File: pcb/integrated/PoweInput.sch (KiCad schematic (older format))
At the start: 35 parts, among them J8001 Conn_01x02_Female, Q8001 Q_NMOS_GDS, Q8002 Q_NMOS_GDS, U8001 SN74LVC1T45DBV, U8002 ADuM5230, U8003 ACS730

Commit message: schematic fixes and component placement
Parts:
- removed U8001: SN74LVC1T45DBV, Package_TO_SOT_SMD:SOT-23-6, symbol Logic_LevelTranslator:SN74LVC1T45DBV
- added C8005: 0.47u, Capacitor_SMD:C_0402_1005Metric, symbol Device:C
- added R8013: 10k, Resistor_SMD:R_0603_1608Metric, symbol Device:R
- added U8001: 74LVC2T45DC, Package_SO:VSSOP-8_2.3x2mm_P0.5mm, symbol Logic_LevelTranslator:74LVC2T45DC
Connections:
- net labels added: SUPPLY_EN1, SUPPLY_EN2
- net labels removed: +3V3D, SUPPLY_EN
- wire segments 135 -> 142
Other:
- moved on the sheet: C8001, R8001
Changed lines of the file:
@@
 Connection ~ 5250 2100
-$Comp
-L Logic_LevelTranslator:SN74LVC1T45DBV U8001
-U 1 1 5D74803E
-P 2350 6300
-F 0 "U8001" H 2791 6346 50  0000 L CNN
-F 1 "SN74LVC1T45DBV" H 2550 5900 50  0000 L CNN
-F 2 "Package_TO_SOT_SMD:SOT-23-6" H 2350 5850 50  0001 C CNN
-F 3 "http://www.ti.com/lit/ds/symlink/sn74lvc1t45.pdf" H 1450 5650 50  0001 C CNN
-	1    2350 6300
-	1    0    0    -1
-$EndComp
 $Comp
 L Device:C C?
 U 1 1 5D748AFA
-P 1800 5500
+P 1250 4800
 AR Path="/5D33C751/5D748AFA" Ref="C?"  Part="1"
 AR Path="/5D688380/5D748AFA" Ref="C8001"  Part="1"
-F 0 "C8001" H 1915 5546 50  0000 L CNN
-F 1 "0.47u" H 1915 5455 50  0000 L CNN
-F 2 "Capacitor_SMD:C_0402_1005Metric" H 1838 5350 50  0001 C CNN
-F 3 "~" H 1800 5500 50  0001 C CNN
-	1    1800 5500
+F 0 "C8001" H 1365 4846 50  0000 L CNN
+F 1 "0.47u" H 1365 4755 50  0000 L CNN
+F 2 "Capacitor_SMD:C_0402_1005Metric" H 1288 4650 50  0001 C CNN
+F 3 "~" H 1250 4800 50  0001 C CNN
+	1    1250 4800
 	1    0    0    -1
 $EndComp
@@
 L power:GND #PWR08004
 U 1 1 5D748F7A
-P 2350 6750
-F 0 "#PWR08004" H 2350 6500 50  0001 C CNN
-F 1 "GND" H 2355 6577 50  0000 C CNN
-F 2 "" H 2350 6750 50  0001 C CNN
-F 3 "" H 2350 6750 50  0001 C CNN
-	1    2350 6750
+P 2350 6950
+F 0 "#PWR08004" H 2350 6700 50  0001 C CNN
+F 1 "GND" H 2500 6900 50  0000 C CNN
+F 2 "" H 2350 6950 50  0001 C CNN
+F 3 "" H 2350 6950 50  0001 C CNN
+	1    2350 6950
 	1    0    0    -1
 $EndComp
@@
 	1    0    0    -1
 $EndComp
-$Comp
-L power:GND #PWR08008
-U 1 1 5D74A979
-P 4000 6500
-F 0 "#PWR08008" H 4000 6250 50  0001 C CNN
-F 1 "GND" H 4005 6327 50  0000 C CNN
-F 2 "" H 4000 6500 50  0001 C CNN
-F 3 "" H 4000 6500 50  0001 C CNN
-	1    4000 6500
-	1    0    0    -1
-$EndComp
-Wire Wire Line
-	4000 6400 4000 6500
-Wire Wire Line
-	4000 6400 4300 6400
 Wire Wire Line
 	4300 6300 2750 6300
@@
 L power:GND #PWR08002
 U 1 1 5D755B60
-P 1800 5700
-F 0 "#PWR08002" H 1800 5450 50  0001 C CNN
-F 1 "GND" H 1805 5527 50  0000 C CNN
-F 2 "" H 1800 5700 50  0001 C CNN
-F 3 "" H 1800 5700 50  0001 C CNN
-	1    1800 5700
-	1    0    0    -1
-$EndComp
-Wire Wire Line
-	1800 5300 1800 5350
-Wire Wire Line
-	1800 5650 1800 5700
-Wire Wire Line
-	2350 6700 2350 6750
+P 1250 5000
+F 0 "#PWR08002" H 1250 4750 50  0001 C CNN
+F 1 "GND" H 1255 4827 50  0000 C CNN
+F 2 "" H 1250 5000 50  0001 C CNN
+F 3 "" H 1250 5000 50  0001 C CNN
+	1    1250 5000
+	1    0    0    -1
+$EndComp
+Wire Wire Line
+	1250 4600 1250 4650
+Wire Wire Line
+	1250 4950 1250 5000
 $Comp
 L power:+3V3 #PWR08003
 U 1 1 5D75B234
-P 1900 6500
-F 0 "#PWR08003" H 1900 6350 50  0001 C CNN
-F 1 "+3V3" V 1915 6628 50  0000 L CNN
-F 2 "" H 1900 6500 50  0001 C CNN
-F 3 "" H 1900 6500 50  0001 C CNN
-	1    1900 6500
-	0    -1   -1   0
-$EndComp
-Wire Wire Line
-	1950 6500 1900 6500
+P 1250 4600
+F 0 "#PWR08003" H 1250 4450 50  0001 C CNN
+F 1 "+3V3" V 1265 4728 50  0000 L CNN
+F 2 "" H 1250 4600 50  0001 C CNN
+F 3 "" H 1250 4600 50  0001 C CNN
+	1    1250 4600
+	1    0    0    -1
+$EndComp
 Wire Wire Line
 	3850 6900 3850 6800
@@
 	1    0    0    -1
 $EndComp
-Text GLabel 1150 6300 0    50   Input ~ 0
-SUPPLY_EN
+Text GLabel 1100 6500 0    50   Input ~ 0
+SUPPLY_EN1
 Wire Wire Line
 	6100 6400 6100 6450
@@
 L Device:R R?
 U 1 1 5D7A4D67
-P 1300 6650
+P 1250 6850
 AR Path="/5D33C751/5D7A4D67" Ref="R?"  Part="1"
 AR Path="/5D688380/5D7A4D67" Ref="R8001"  Part="1"
-F 0 "R8001" H 1370 6696 50  0000 L CNN
-F 1 "10k" H 1370 6605 50  0000 L CNN
-F 2 "Resistor_SMD:R_0603_1608Metric" V 1230 6650 50  0001 C CNN
-F 3 "~" H 1300 6650 50  0001 C CNN
-	1    1300 6650
+F 0 "R8001" H 1320 6896 50  0000 L CNN
+F 1 "10k" H 1320 6805 50  0000 L CNN
+F 2 "Resistor_SMD:R_0603_1608Metric" V 1180 6850 50  0001 C CNN
+F 3 "~" H 1250 6850 50  0001 C CNN
+	1    1250 6850
 	1    0    0    1
 $EndComp
 Wire Wire Line
-	1300 6500 1300 6300
-Wire Wire Line
-	1300 6300 1950 6300
-Wire Wire Line
-	1300 6300 1150 6300
-Connection ~ 1300 6300
+	1250 6700 1250 6500
+Wire Wire Line
+	1250 6500 1100 6500
+Connection ~ 1250 6500
 $Comp
 L power:GND #PWR08001
 U 1 1 5D7AE718
-P 1300 6850
-F 0 "#PWR08001" H 1300 6600 50  0001 C CNN
-F 1 "GND" H 1305 6677 50  0000 C CNN
-F 2 "" H 1300 6850 50  0001 C CNN
-F 3 "" H 1300 6850 50  0001 C CNN
-	1    1300 6850
-	1    0    0    -1
-$EndComp
-Wire Wire Line
-	1300 6800 1300 6850
+P 1250 7050
+F 0 "#PWR08001" H 1250 6800 50  0001 C CNN
+F 1 "GND" H 1255 6877 50  0000 C CNN
+F 2 "" H 1250 7050 50  0001 C CNN
+F 3 "" H 1250 7050 50  0001 C CNN
+	1    1250 7050
+	1    0    0    -1
+$EndComp
+Wire Wire Line
+	1250 7000 1250 7050
 $Comp
 L wbraun_ic_lib:ACS730 U8003
@@
 Text GLabel 7700 5100 0    50   Input ~ 0
 IL_ZERO
-Text GLabel 1800 5300 0    50   Input ~ 0
-+3V3D
-Text GLabel 2250 5800 1    50   Input ~ 0
-+3V3D
 $Comp
 L Device:R R?
@@
 Wire Wire Line
 	9700 3300 9700 3500
-Text Label 5000 1950 0    50   ~ 0
-VIN
 Text Label 5450 6750 0    50   ~ 0
 GATE2+
@@
 Wire Wire Line
 	9700 3900 9700 4150
+Text GLabel 5000 1950 2    50   Input ~ 0
+VIN
+$Comp
+L Logic_LevelTranslator:74LVC2T45DC U8001
+U 1 1 5D8F7B18
+P 2350 6400
+F 0 "U8001" H 2650 6900 50  0000 C CNN
+F 1 "74LVC2T45DC" H 1900 5950 50  0000 C CNN
+F 2 "Package_SO:VSSOP-8_2.3x2mm_P0.5mm" H 2350 5550 50  0001 C CNN
+F 3 "https://assets.nexperia.com/documents/data-sheet/74LVC_LVCH2T45.pdf" H 2600 6150 50  0001 C CNN
+	1    2350 6400
+	1    0    0    -1
+$EndComp
+Wire Wire Line
+	2950 6400 2950 6500
+Wire Wire Line
+	2950 6500 2750 6500
+Wire Wire Line
+	2950 6400 4300 6400
+$Comp
+L power:+3V3 #PWR0180
+U 1 1 5D909304
+P 2250 5800
+F 0 "#PWR0180" H 2250 5650 50  0001 C CNN
+F 1 "+3V3" V 2265 5928 50  0000 L CNN
+F 2 "" H 2250 5800 50  0001 C CNN
+F 3 "" H 2250 5800 50  0001 C CNN
+	1    2250 5800
+	1    0    0    -1
+$EndComp
+$Comp
+L Device:C C?
+U 1 1 5D90B099
+P 1950 4800
+AR Path="/5D33C751/5D90B099" Ref="C?"  Part="1"
+AR Path="/5D688380/5D90B099" Ref="C8005"  Part="1"
+F 0 "C8005" H 2065 4846 50  0000 L CNN
+F 1 "0.47u" H 2065 4755 50  0000 L CNN
+F 2 "Capacitor_SMD:C_0402_1005Metric" H 1988 4650 50  0001 C CNN
+F 3 "~" H 1950 4800 50  0001 C CNN
+	1    1950 4800
+	1    0    0    -1
+$EndComp
+$Comp
+L power:GND #PWR0181
+U 1 1 5D90B09F
+P 1950 5000
+F 0 "#PWR0181" H 1950 4750 50  0001 C CNN
+F 1 "GND" H 1955 4827 50  0000 C CNN
+F 2 "" H 1950 5000 50  0001 C CNN
+F 3 "" H 1950 5000 50  0001 C CNN
+	1    1950 5000
+	1    0    0    -1
+$EndComp
+Wire Wire Line
+	1950 4600 1950 4650
+Wire Wire Line
+	1950 4950 1950 5000
+$Comp
+L power:+5V #PWR0182
+U 1 1 5D914E5D
+P 1950 4600
+F 0 "#PWR0182" H 1950 4450 50  0001 C CNN
+F 1 "+5V" H 1965 4773 50  0000 C CNN
+F 2 "" H 1950 4600 50  0001 C CNN
+F 3 "" H 1950 4600 50  0001 C CNN
+	1    1950 4600
+	1    0    0    -1
+$EndComp
+Wire Wire Line
+	2350 6900 2350 6950
+Wire Wire Line
+	1250 6500 1950 6500
+$Comp
+L Device:R R?
+U 1 1 5D921AF7
+P 1250 6000
+AR Path="/5D33C751/5D921AF7" Ref="R?"  Part="1"
+AR Path="/5D688380/5D921AF7" Ref="R8013"  Part="1"
+F 0 "R8013" H 1320 6046 50  0000 L CNN
+F 1 "10k" H 1320 5955 50  0000 L CNN
+F 2 "Resistor_SMD:R_0603_1608Metric" V 1180 6000 50  0001 C CNN
+F 3 "~" H 1250 6000 50  0001 C CNN
+	1    1250 6000
+	1    0    0    1
+$EndComp
+$Comp
+L power:GND #PWR0183
+U 1 1 5D921E4F
+P 1250 5800
+F 0 "#PWR0183" H 1250 5550 50  0001 C CNN
+F 1 "GND" H 1255 5627 50  0000 C CNN
+F 2 "" H 1250 5800 50  0001 C CNN
+F 3 "" H 1250 5800 50  0001 C CNN
+	1    1250 5800
+	-1   0    0    1
+$EndComp
+Wire Wire Line
+	1950 6300 1250 6300
+Wire Wire Line
+	1250 6300 1250 6150
+Wire Wire Line
+	1250 6300 1100 6300
+Connection ~ 1250 6300
+Text GLabel 1100 6300 0    50   Input ~ 0
+SUPPLY_EN2
+Wire Wire Line
+	1250 5800 1250 5850
+$Comp
+L power:+3V3 #PWR0184
+U 1 1 5D931E8A
+P 1900 6700
+F 0 "#PWR0184" H 1900 6550 50  0001 C CNN
+F 1 "+3V3" V 1915 6828 50  0000 L CNN
+F 2 "" H 1900 6700 50  0001 C CNN
+F 3 "" H 1900 6700 50  0001 C CNN
+	1    1900 6700
+	0    -1   -1   0
+$EndComp
+Wire Wire Line
+	1950 6700 1900 6700
 $EndSCHEMATC

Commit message: revised power input schematic
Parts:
- removed C8005, C8006, C8007: 0.47u, Capacitor_SMD:C_0402_1005Metric, symbol Device:C
- removed C8009: 10u, Capacitor_SMD:C_0603_1608Metric, symbol Device:C
- removed C8010: 0.47u, Capacitor_SMD:C_0603_1608Metric, symbol Device:C
- removed C8011: 1u, Capacitor_SMD:C_2220_5650Metric_Pad1.97x5.40mm_HandSolder, symbol Device:C
- removed D8001: D_Bridge_+AA-, wbraun_smd:Diode-GBJ-Vertical, symbol Device:D_Bridge_+AA-
- removed FB8002: Ferrite_Bead_Small, Inductor_SMD:L_0805_2012Metric, symbol Device:Ferrite_Bead_Small
- removed L8001: CM_CHOKE, wbraun_smd:744824622, symbol wbraun_ic_lib:CM_CHOKE
- removed Q8002: Q_NMOS_GDS, Package_TO_SOT_THT:TO-247-3_Vertical, symbol Device:Q_NMOS_GDS
- removed U8001: 74LVC2T45DC, Package_SO:VSSOP-8_2.3x2mm_P0.5mm, symbol Logic_LevelTranslator:74LVC2T45DC
- removed U8002: ADuM5230, Package_SO:SOIC-16W_7.5x10.3mm_P1.27mm, symbol wbraun_ic_lib:ADuM5230
- added D8001: D, Package_TO_SOT_THT:TO-247-2_Vertical, symbol Device:D
- added J8002: mounting-hole-grounded, wbraun_smd:OMNI-UNI-30-50-D, symbol wbraun_ic_lib:mounting-hole-grounded
- added Q8002: 2N7002, Package_TO_SOT_SMD:SOT-23, symbol Transistor_FET:2N7002
- added Q8003: Q_NMOS_GDS, Package_TO_SOT_THT:TO-247-3_Vertical, symbol Device:Q_NMOS_GDS
- added U8001: VOM1271, Package_SO:SO-4_4.4x4.3mm_P2.54mm, symbol wbraun_ic_lib:VOM1271
- added U8002: UCC5350SB, Package_SO:SOIC-8_3.9x4.9mm_P1.27mm, symbol wbraun_ic_lib:UCC5350SB
- C8001: value 0.47u -> 4.7u; footprint Capacitor_SMD:C_0402_1005Metric -> Capacitor_SMD:C_0805_2012Metric
- C8004: value 10u -> 0.47u
- C8008: footprint Capacitor_THT:C_Rect_L31.5mm_W20.0mm_P27.50mm_MKS4 -> Capacitor_THT:C_Rect_L33.0mm_W13.0mm_P27.50mm_MKS4
- R8001: value 10k -> 100; footprint Resistor_SMD:R_0603_1608Metric -> Resistor_SMD:R_0402_1005Metric
- R8002: value 4.7 -> 4.7K; footprint Resistor_SMD:R_0603_1608Metric -> Resistor_SMD:R_0402_1005Metric
- R8003: value 4.7 -> 100; footprint Resistor_SMD:R_0603_1608Metric -> Resistor_SMD:R_0402_1005Metric
- R8004: value 10k -> 4.7K; footprint Resistor_SMD:R_0603_1608Metric -> Resistor_SMD:R_0402_1005Metric
- R8005: value 10k -> 1; footprint Resistor_SMD:R_0603_1608Metric -> Resistor_SMD:R_0805_2012Metric
- R8006: value 4.7 -> 1; footprint Package_TO_SOT_THT:TO-247-2_Vertical -> Resistor_SMD:R_0805_2012Metric
- R8013: value 10k -> 4.7K
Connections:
- net labels added: DRIVE_AUX+, DRIVE_AUX-, G1, G2, S1, VBUS, Vgd
- net labels removed: GATE-, GATE1+, GATE2+, SUPPLY_EN2, SW_NODE
- wire segments 142 -> 109
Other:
- moved on the sheet: C8002, C8003, C8008, F8001, J8001, L8002, Q8001, R8014, U8003

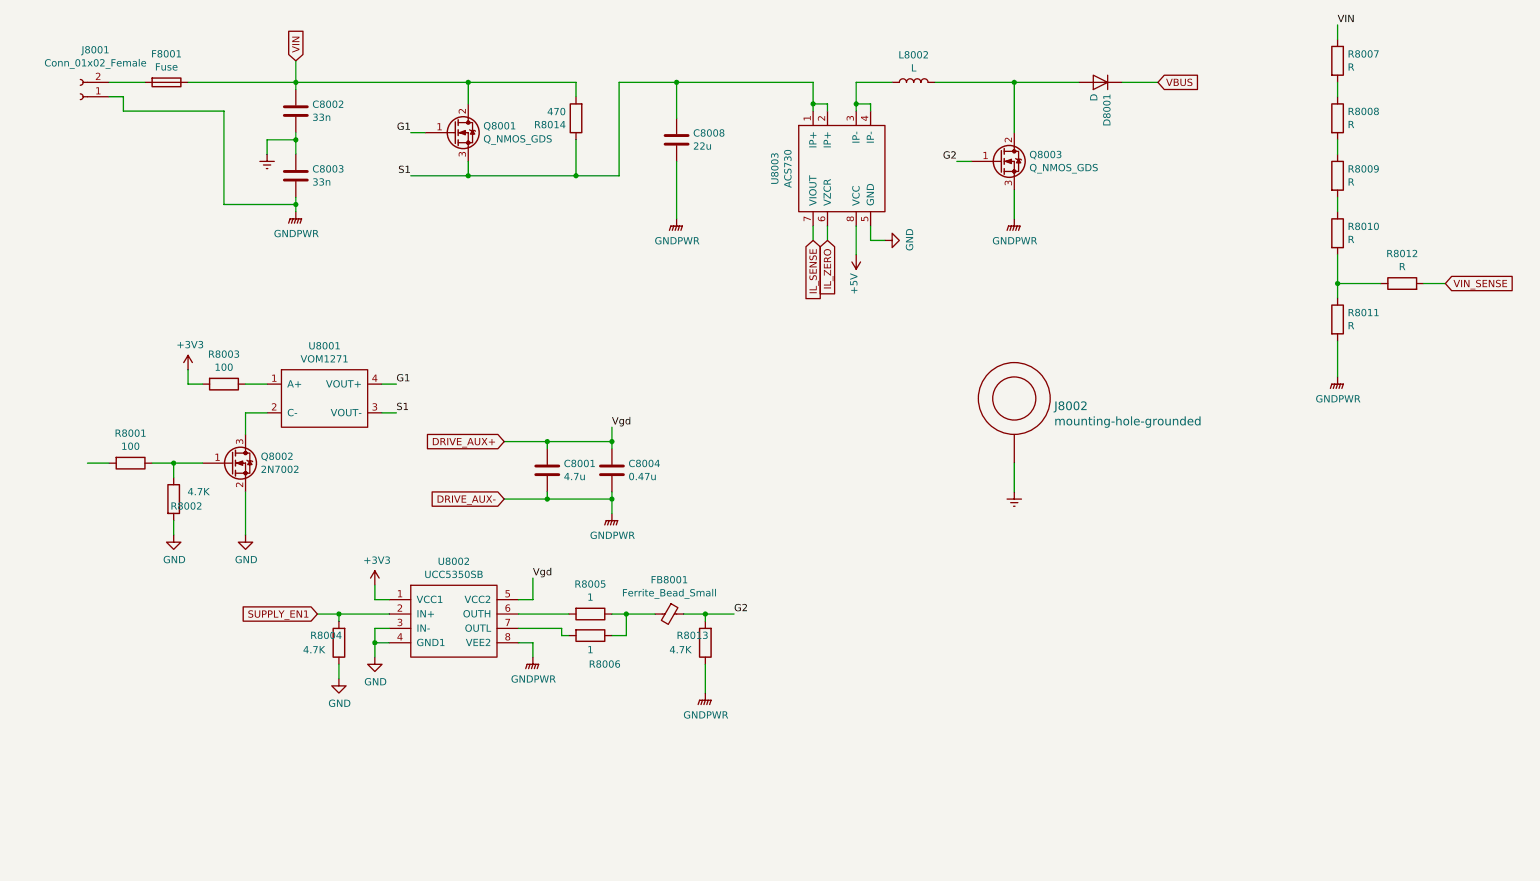
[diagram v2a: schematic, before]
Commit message: routing, all componens placed on PCB
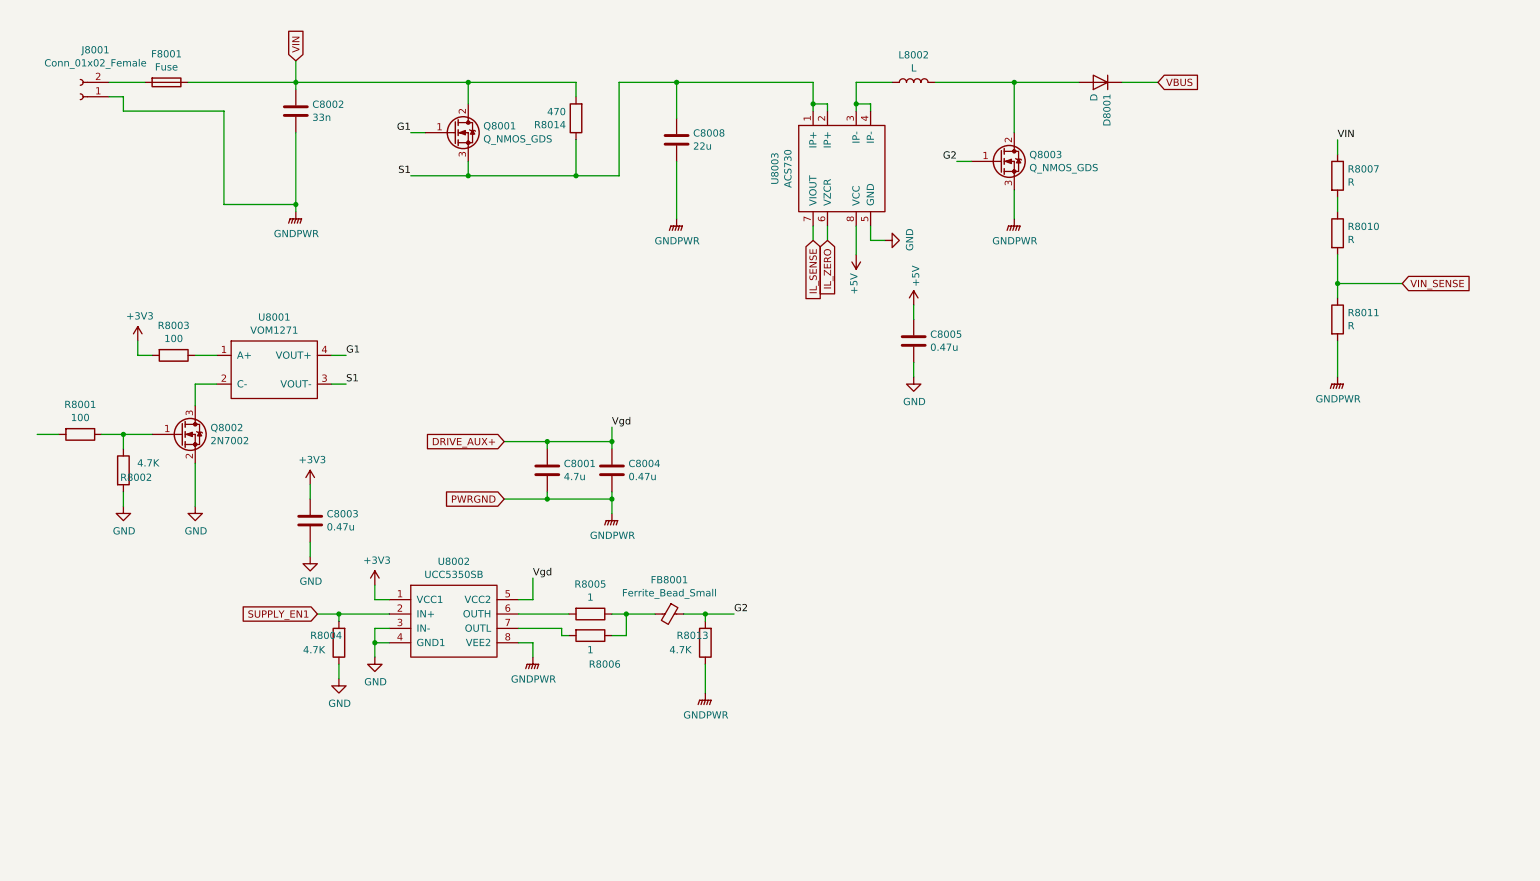
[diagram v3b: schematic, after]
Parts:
- removed J8002: mounting-hole-grounded, wbraun_smd:OMNI-UNI-30-50-D, symbol wbraun_ic_lib:mounting-hole-grounded
- removed R8008, R8009: R, Resistor_SMD:R_0805_2012Metric, symbol Device:R
- removed R8012: R, Resistor_SMD:R_0603_1608Metric, symbol Device:R
- added C8005: 0.47u, Capacitor_SMD:C_0603_1608Metric, symbol Device:C
- C8003: value 33n -> 0.47u; footprint Capacitor_THT:C_Rect_L18.0mm_W7.0mm_P15.00mm_FKS3_FKP3 -> Capacitor_SMD:C_0603_1608Metric
- D8001, R8014: footprint Package_TO_SOT_THT:TO-247-2_Vertical -> wbraun_smd:TO-247_2_horizontal_under
- Q8001, Q8003: footprint Package_TO_SOT_THT:TO-247-3_Vertical -> wbraun_smd:TO-247_3_horizontal_under
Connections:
- net +3V3: now also C8003.1
- net +5V: now also C8005.1
- net GND: now also C8003.2, C8005.2
- net GNDPWR: now also C8002.2; no longer C8003.2
- net VIN_SENSE: now also R8010.2, R8011.1
- net at R8007.2: now also R8010.1
- removed net Earth: C8002.2, C8003.1
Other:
- moved on the sheet: Q8002, R8001, R8002, R8003, R8007, U8001

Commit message: routing progress
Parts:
- removed J8001: Conn_01x02_Female, wbraun_smd:Anderson_PP45_2x1, symbol Connector:Conn_01x02_Female
- added J8001: Conn_01x03_Female, wbraun_smd:Terminal-block-plug_3x1_5mm-pitch, symbol Connector:Conn_01x03_Female
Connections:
- net GNDPWR: now also J8001.2 (Pin_2)
- net at F8001.2: now also J8001.1 (Pin_1)
- new net Earth: J8001.3 (Pin_3)
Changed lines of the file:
@@
-$EndComp
-$Comp
-L Connector:Conn_01x02_Female J?
-U 1 1 5D688D73
-P 950 2200
-AR Path="/5D33C751/5D688D73" Ref="J?"  Part="1"
-AR Path="/5D688380/5D688D73" Ref="J8001"  Part="1"
-F 0 "J8001" H 844 1875 50  0000 C CNN
-F 1 "Conn_01x02_Female" H 844 1966 50  0000 C CNN
-F 2 "wbraun_smd:Anderson_PP45_2x1" H 950 2200 50  0001 C CNN
-F 3 "~" H 950 2200 50  0001 C CNN
-	1    950  2200
-	-1   0    0    1
 $EndComp
 $Comp
@@
 Wire Wire Line
 	5100 2650 5100 3050
-Wire Wire Line
-	1150 2200 1250 2200
-Wire Wire Line
-	1250 2200 1250 2300
 Text GLabel 2600 5800 0    50   Input ~ 0
 SUPPLY_EN1
@@
 Wire Wire Line
 	1700 2100 2450 2100
-Wire Wire Line
-	1250 2300 1950 2300
-Wire Wire Line
-	1950 2300 1950 2950
 Text GLabel 6150 3200 3    50   Input ~ 0
 IL_ZERO
@@
 	1    0    0    -1
 $EndComp
+$Comp
+L Connector:Conn_01x03_Female J8001
+U 1 1 5DBE4336
+P 950 2200
+F 0 "J8001" H 842 2485 50  0000 C CNN
+F 1 "Conn_01x03_Female" H 842 2394 50  0000 C CNN
+F 2 "wbraun_smd:Terminal-block-plug_3x1_5mm-pitch" H 950 2200 50  0001 C CNN
+F 3 "~" H 950 2200 50  0001 C CNN
+	1    950  2200
+	-1   0    0    -1
+$EndComp
+Wire Wire Line
+	1150 2200 1950 2200
+Wire Wire Line
+	1950 2200 1950 2950
+Wire Wire Line
+	1150 2300 1150 2500
+$Comp
+L power:Earth #PWR?
+U 1 1 5DBEA1A2
+P 1150 2500
+AR Path="/5DBEA1A2" Ref="#PWR?"  Part="1"
+AR Path="/5D688380/5DBEA1A2" Ref="#PWR0129"  Part="1"
+F 0 "#PWR0129" H 1150 2250 50  0001 C CNN
+F 1 "Earth" H 1150 2350 50  0001 C CNN
+F 2 "" H 1150 2500 50  0001 C CNN
+F 3 "~" H 1150 2500 50  0001 C CNN
+	1    1150 2500
+	1    0    0    -1
+$EndComp

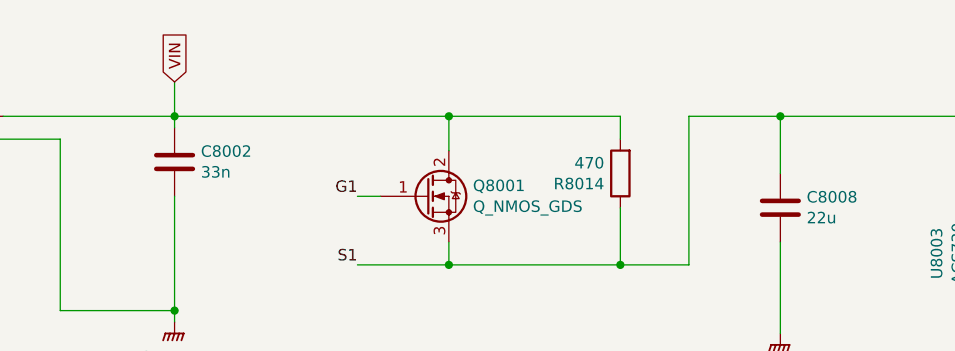
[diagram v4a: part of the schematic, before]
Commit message: redid power planes
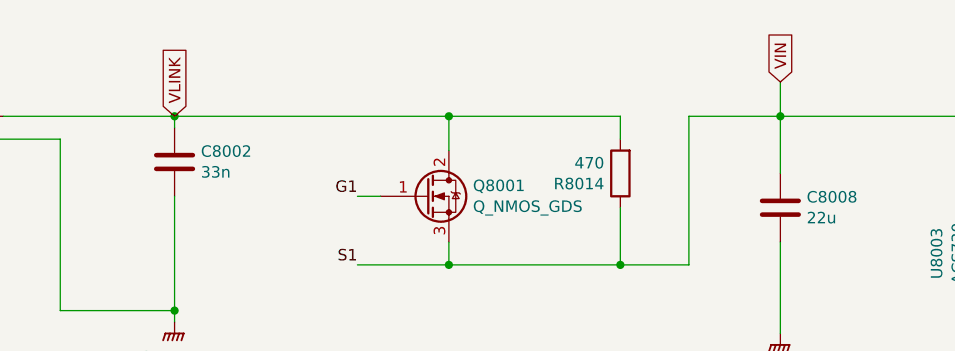
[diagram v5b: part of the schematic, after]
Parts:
- R8004: footprint Resistor_SMD:R_0402_1005Metric -> Resistor_SMD:R_0603_1608Metric
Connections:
- net S1 is gone; now on net VIN: C8008.1, Q8001.3 (S), R8014.1, U8001.3 (VOUT-), U8003.1 (IP+), U8003.2 (IP+)
- net VIN: no longer C8002.1, F8001.1, Q8001.2 (D), R8014.2
- new net VLINK: C8002.1, F8001.1, Q8001.2 (D), R8014.2
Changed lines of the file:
@@
 Wire Wire Line
 	9700 3900 9700 4150
-Text GLabel 2450 1950 1    50   Input ~ 0
+Text GLabel 5100 1950 1    50   Input ~ 0
 VIN
 $Comp
@@
 $EndComp
 Wire Wire Line
-	2450 1950 2450 2100
+	5100 1950 5100 2100
 Connection ~ 2450 2100
 Wire Wire Line
@@
 F 0 "R8004" H 2950 5950 50  0000 R CNN
 F 1 "4.7K" H 3000 6050 50  0000 R CNN
-F 2 "Resistor_SMD:R_0402_1005Metric" V 2680 6000 50  0001 C CNN
+F 2 "Resistor_SMD:R_0603_1608Metric" V 2680 6000 50  0001 C CNN
 F 3 "~" H 2750 6000 50  0001 C CNN
 	1    2750 6000
@@
 	1    0    0    -1
 $EndComp
+Text GLabel 2450 2100 1    50   Input ~ 0
+VLINK
 $EndSCHEMATC

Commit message: PCB routing finihsed, ready for design review
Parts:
- R8005, R8006: value 1 -> 4.7
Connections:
- net CHARGE_SW: now reaches R8001.2
- net SUPPLY_EN1 renamed BOOST_SW
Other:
- moved on the sheet: C8001, C8003, C8004, FB8001, Q8002, R8001, R8002, R8003, R8004, R8005, R8006, R8013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
